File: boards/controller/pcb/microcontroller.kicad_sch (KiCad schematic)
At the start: 21 parts, among them SW3001 SW_Push, SW3002 SW_Push, U3001 STM32U575VITx, X3001 16MHz

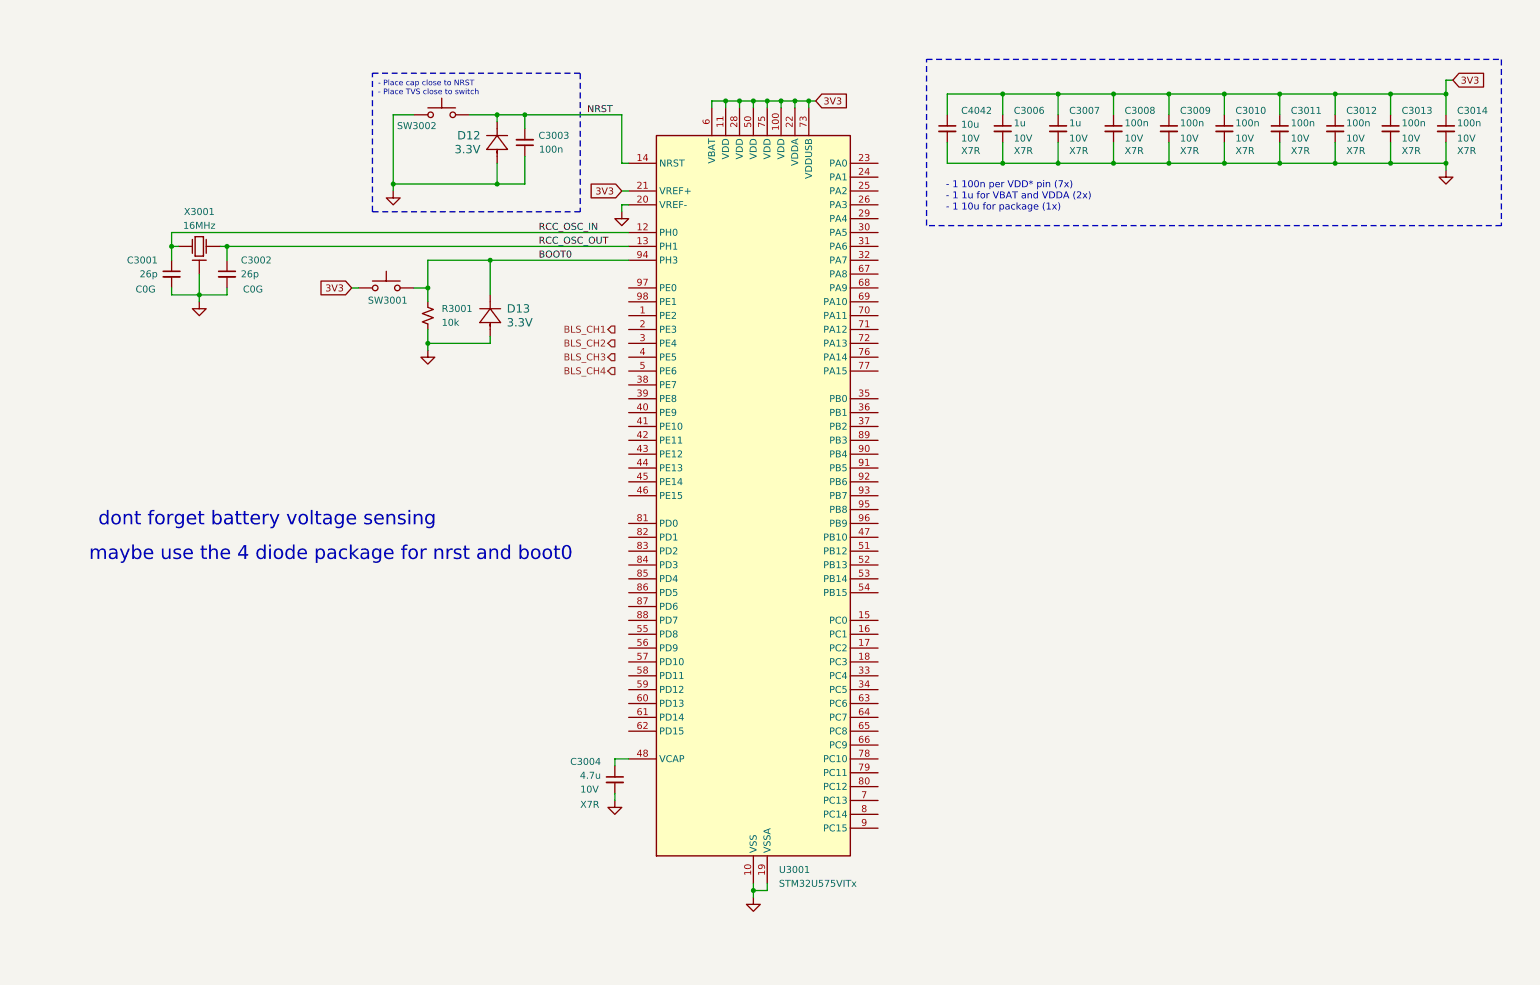
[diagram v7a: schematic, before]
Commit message: controller: pcb: Update schematic
- add VBAT sense circuit
- add BLS power pmos
- assign BLS GPIO

Signed-off-by: Nicholas Loehrke <nicholasnloehrke@gmail.com>
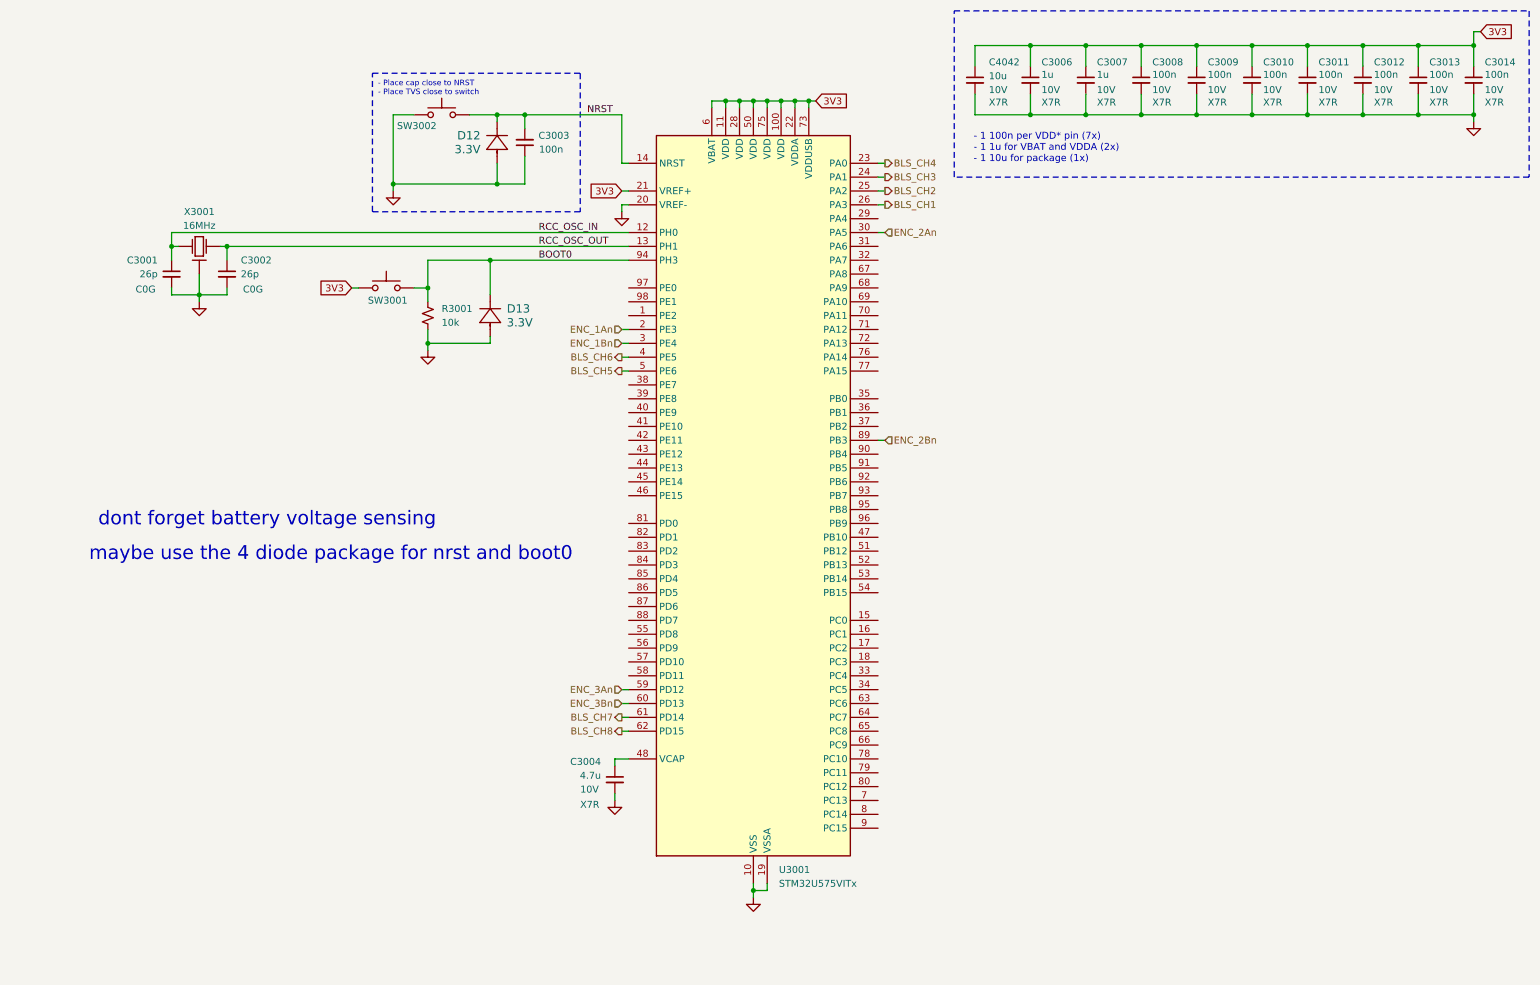
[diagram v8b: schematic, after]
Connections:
- net BLS_CH1: now also U3001.26 (PA3)
- net BLS_CH2: now also U3001.25 (PA2)
- net BLS_CH3: now also U3001.24 (PA1)
- net BLS_CH4: now also U3001.23 (PA0)
- net ENC_1An: now reaches U3001.2 (PE3)
- net ENC_1Bn: now reaches U3001.3 (PE4)
- net ENC_2An: now reaches U3001.30 (PA5)
- net BLS_CH6: now reaches U3001.4 (PE5)
- net BLS_CH5: now reaches U3001.5 (PE6)
- net ENC_3An: now reaches U3001.59 (PD12)
- net ENC_3Bn: now reaches U3001.60 (PD13)
- net BLS_CH7: now reaches U3001.61 (PD14)
- net BLS_CH8: now reaches U3001.62 (PD15)
- net ENC_2Bn: now reaches U3001.89 (PB3)
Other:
- moved on the sheet: C3006, C3007, C3008, C3009, C3010, C3011, C3012, C3013, C3014, C4042
